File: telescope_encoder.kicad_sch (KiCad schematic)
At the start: 10 parts, among them J1 Conn_01x04_Male, J2 Conn_01x02_Male, U1 AS5048B

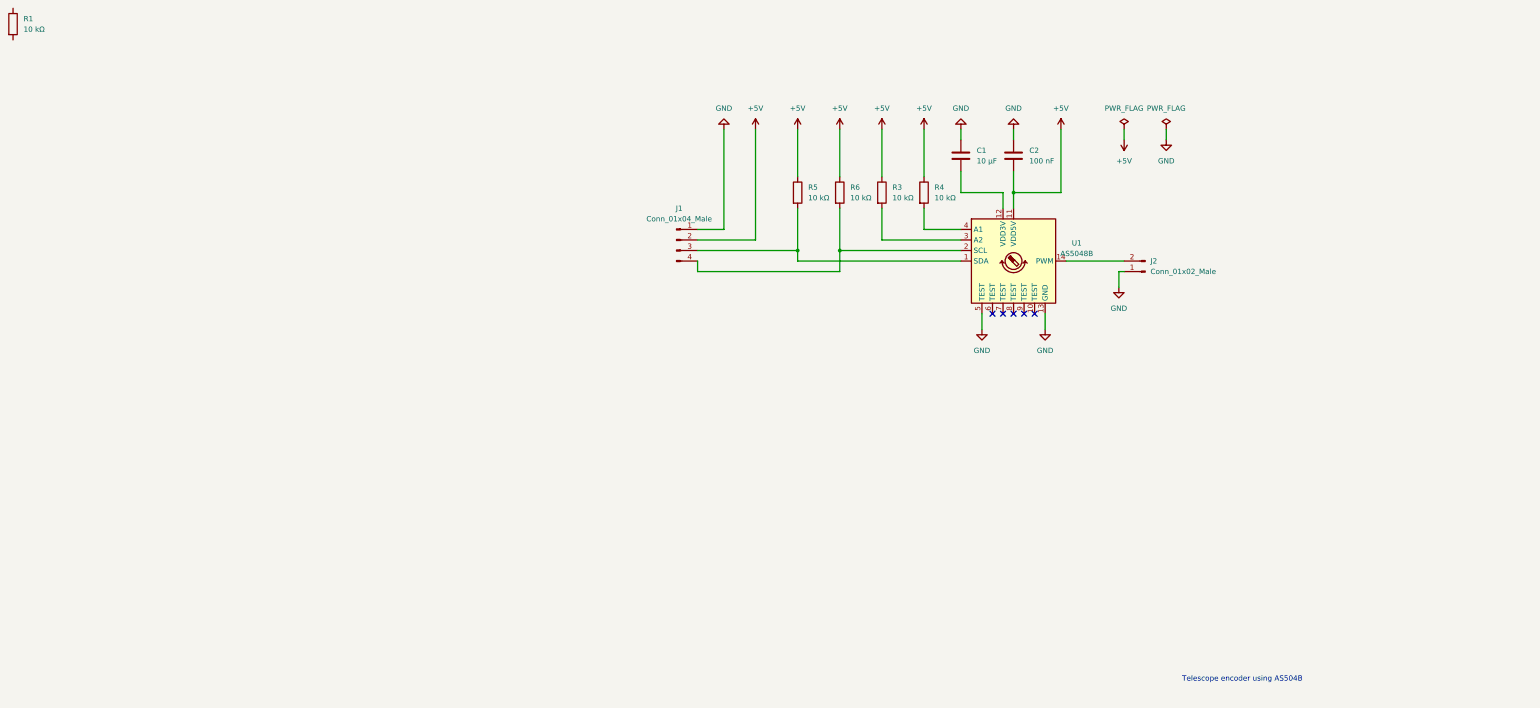
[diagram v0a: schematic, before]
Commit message: Updated PCB
The tracks need to be checked for parasitic capacitance issues
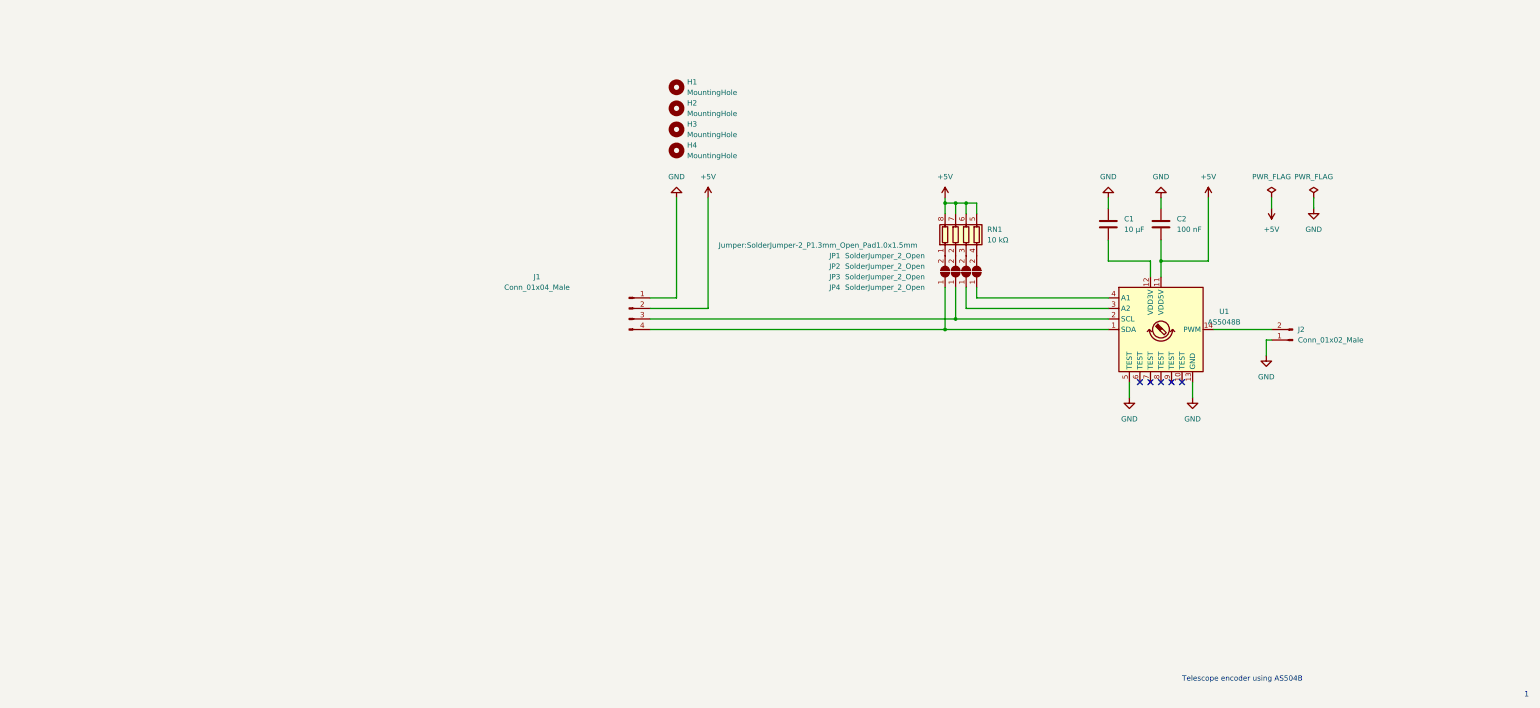
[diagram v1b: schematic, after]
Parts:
- removed R1, R3, R4, R5, R6: 10 kΩ, Resistor_SMD:R_1206_3216Metric_Pad1.30x1.75mm_HandSolder, symbol Device:R
- added H1, H2, H3, H4: MountingHole, MountingHole:MountingHole_2.2mm_M2_DIN965, symbol Mechanical:MountingHole
- added JP1, JP2, JP3, JP4: SolderJumper_2_Open, Jumper:SolderJumper-2_P1.3mm_Open_Pad1.0x1.5mm, symbol Jumper:SolderJumper_2_Open
- added RN1: 10 kΩ, Resistor_SMD:R_Array_Convex_4x1206, symbol Device:R_Pack04
- C2: footprint Capacitor_THT:C_Disc_D7.0mm_W2.5mm_P5.00mm -> Capacitor_SMD:C_1206_3216Metric_Pad1.33x1.80mm_HandSolder
- J1: footprint Connector_PinHeader_1.27mm:PinHeader_1x04_P1.27mm_Vertical -> Connector_PinHeader_1.27mm:PinHeader_1x04_P1.27mm_Vertical_SMD_Pin1Left
- J2: footprint Connector_PinHeader_1.00mm:PinHeader_1x02_P1.00mm_Vertical -> Connector_PinHeader_1.00mm:PinHeader_1x02_P1.00mm_Vertical_SMD_Pin1Left
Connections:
- net +5V: now also RN1.5 (R4.2), RN1.6 (R3.2), RN1.7 (R2.2), RN1.8 (R1.2)
- net at U1.4 (A1): now also JP4.1 (A)
- net at U1.1 (SDA): now also J1.4 (Pin_4), JP1.1 (A); no longer J1.3 (Pin_3)
- net at U1.2 (SCL): now also J1.3 (Pin_3), JP2.1 (A); no longer J1.4 (Pin_4)
- net at U1.3 (A2): now also JP3.1 (A)
- new net: JP4.2 (B), RN1.4 (R4.1)
- new net: JP1.2 (B), RN1.1 (R1.1)
- new net: JP2.2 (B), RN1.2 (R2.1)
- new net: JP3.2 (B), RN1.3 (R3.1)
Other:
- note added: "1"
- moved on the sheet: C1, C2, J1, J2, U1
